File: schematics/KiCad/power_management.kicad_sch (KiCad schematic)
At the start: 33 parts, among them J3 USB_C, Q1 DMG6601LVT-7, Q2 DMG6601LVT-7, SW4 TL1105SF160R, U4 AP2112K-3.3, U5 MP2615AGQ-Z

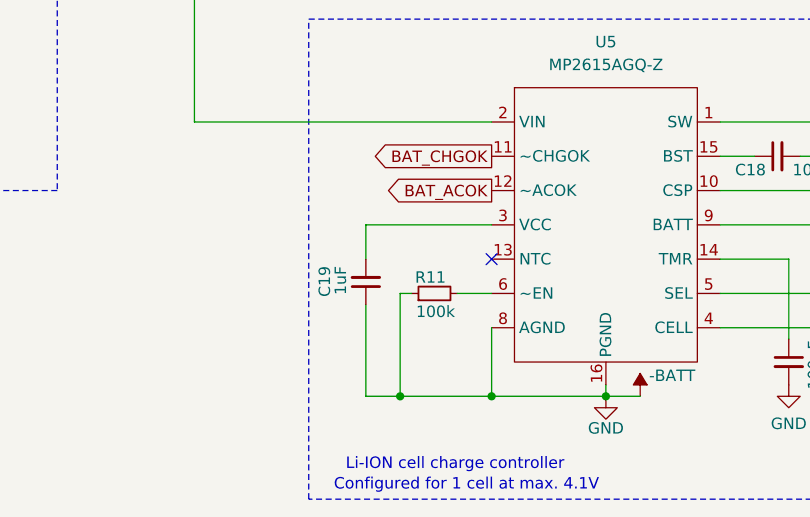
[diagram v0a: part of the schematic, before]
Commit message: wire up thermistor pin on charge controller
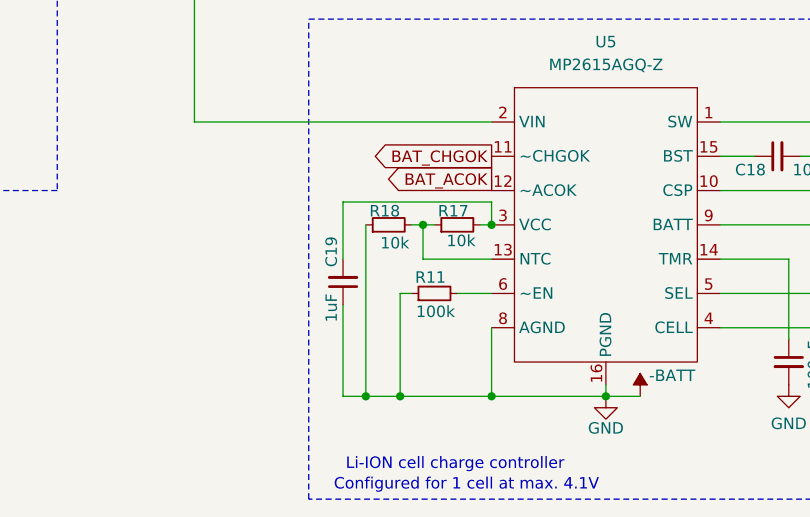
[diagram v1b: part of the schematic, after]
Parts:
- added R17, R18: 10k, Resistor_SMD:R_0603_1608Metric, symbol Device:R_Small
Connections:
- net -BATT: now also R18.1
- net at C19.2, U5.3 (VCC): now also R17.2
- net at U5.13 (NTC): now also R17.1, R18.2
- no-connect marks 1 -> 0
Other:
- moved on the sheet: C19

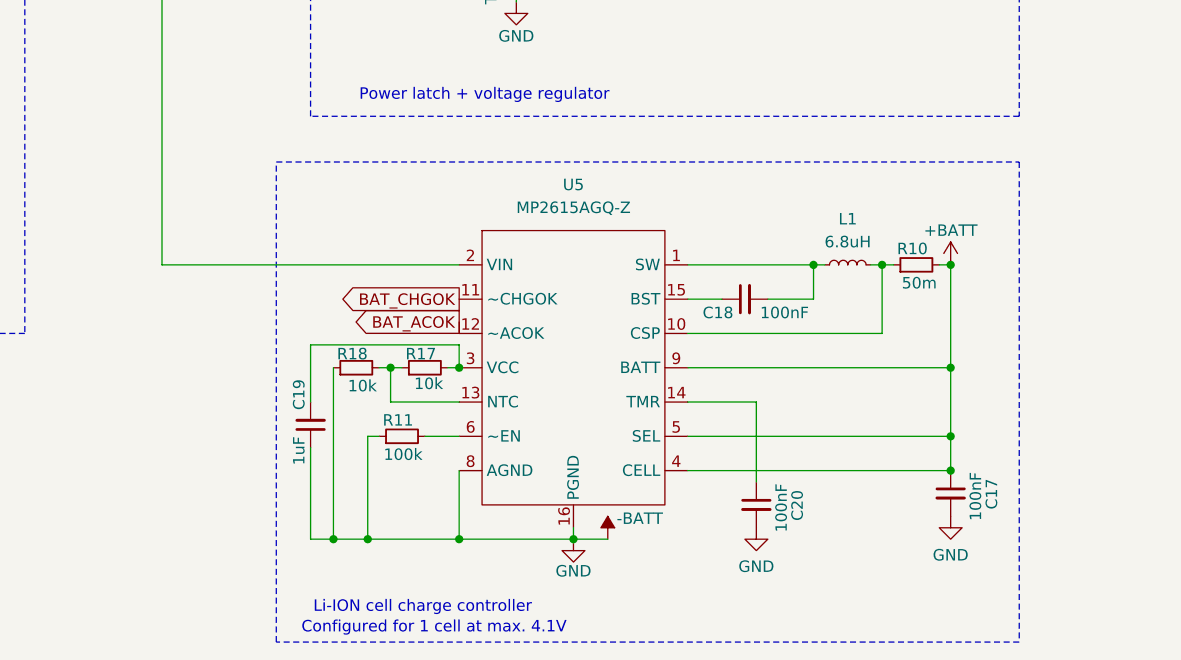
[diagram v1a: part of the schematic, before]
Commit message: set charge time according to datasheet
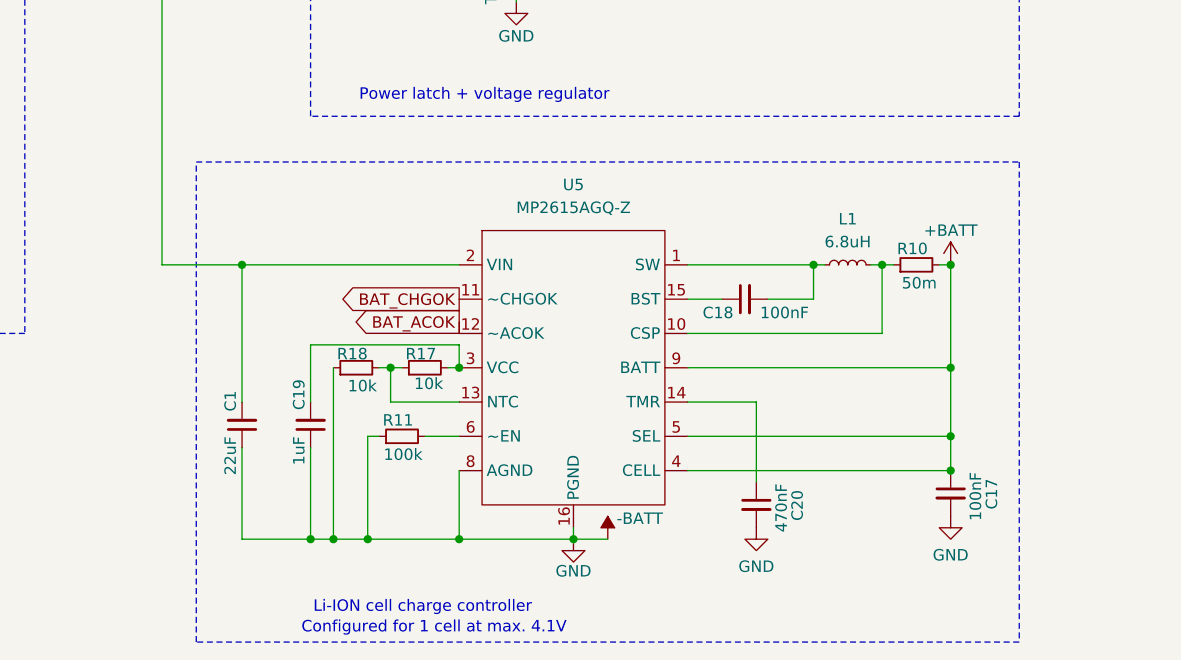
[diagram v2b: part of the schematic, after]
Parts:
- added C1: 22uF, Capacitor_SMD:C_0201_0603Metric, symbol Device:C_Small
- C20: value 100nF -> 470nF
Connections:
- net -BATT: now also C1.1
- net VBUS: now also C1.2
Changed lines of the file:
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@@
 	)
 	(junction
+		(at 100.33 115.57)
+		(diameter 0)
+		(color 0 0 0 0)
+	)
+	(junction
+		(at 107.95 146.05)
+		(diameter 0)
+		(color 0 0 0 0)
+	)
+	(junction
 		(at 91.44 74.93)
 		(diameter 0)
@@
 	(wire
 		(pts
-			(xy 91.44 115.57) (xy 124.46 115.57)
+			(xy 100.33 115.57) (xy 124.46 115.57)
+		)
+		(stroke
+			(width 0)
+			(type default)
+		)
+	)
+	(wire
+		(pts
+			(xy 91.44 115.57) (xy 100.33 115.57)
 		)
 		(stroke
@@
 	(wire
 		(pts
+			(xy 100.33 115.57) (xy 100.33 130.81)
+		)
+		(stroke
+			(width 0)
+			(type default)
+		)
+	)
+	(wire
+		(pts
 			(xy 55.88 90.17) (xy 57.15 90.17)
 		)
@@
 	(wire
 		(pts
+			(xy 100.33 135.89) (xy 100.33 146.05)
+		)
+		(stroke
+			(width 0)
+			(type default)
+		)
+	)
+	(wire
+		(pts
 			(xy 68.58 82.55) (xy 68.58 80.01)
 		)
@@
 	(wire
 		(pts
+			(xy 100.33 146.05) (xy 107.95 146.05)
+		)
+		(stroke
+			(width 0)
+			(type default)
+		)
+	)
+	(wire
+		(pts
 			(xy 140.97 85.09) (xy 140.97 83.82)
 		)
@@
 	)
 	(rectangle
-		(start 104.14 104.14)
+		(start 95.25 104.14)
 		(end 186.69 157.48)
 		(stroke
@@
 	)
 	(symbol
+		(lib_id "Device:C_Small")
+		(at 100.33 133.35 180)
+		(unit 1)
+		(exclude_from_sim no)
+		(in_bom yes)
+		(on_board yes)
+		(dnp no)
+		(property "Reference" "C1"
+			(at 99.06 129.54 90)
+			(effects
+				(font
+					(size 1.27 1.27)
+				)
+				(justify left)
+			)
+		)
+		(property "Value" "22uF"
+			(at 99.06 134.62 90)
+			(effects
+				(font
+					(size 1.27 1.27)
+				)
+				(justify left)
+			)
+		)
+		(property "Footprint" "Capacitor_SMD:C_0201_0603Metric"
+			(at 100.33 133.35 0)
+			(effects
+				(font
+					(size 1.27 1.27)
+				)
+				(hide yes)
+			)
+		)
+		(property "Datasheet" "~"
+			(at 100.33 133.35 0)
+			(effects
+				(font
+					(size 1.27 1.27)
+				)
+				(hide yes)
+			)
+		)
+		(property "Description" "Unpolarized capacitor, small symbol"
+			(at 100.33 133.35 0)
+			(effects
+				(font
+					(size 1.27 1.27)
+				)
+				(hide yes)
+			)
+		)
+		(pin "2"
+		)
+		(pin "1"
+		)
+		(instances
+			(project "leany"
+				(path "/e47b2519-93ca-4a48-9414-ecc253dd35f5/702fc064-eab2-4b82-8f62-a654ccd28f72"
+					(reference "C1")
+					(unit 1)
+				)
+			)
+		)
+	)
+	(symbol
 		(lib_id "Device:C_Polarized_Small")
 		(at 179.07 45.72 0)
@@
 			)
 		)
-		(property "Value" "100nF"
+		(property "Value" "470nF"
 			(at 160.274 145.288 90)
 			(effects

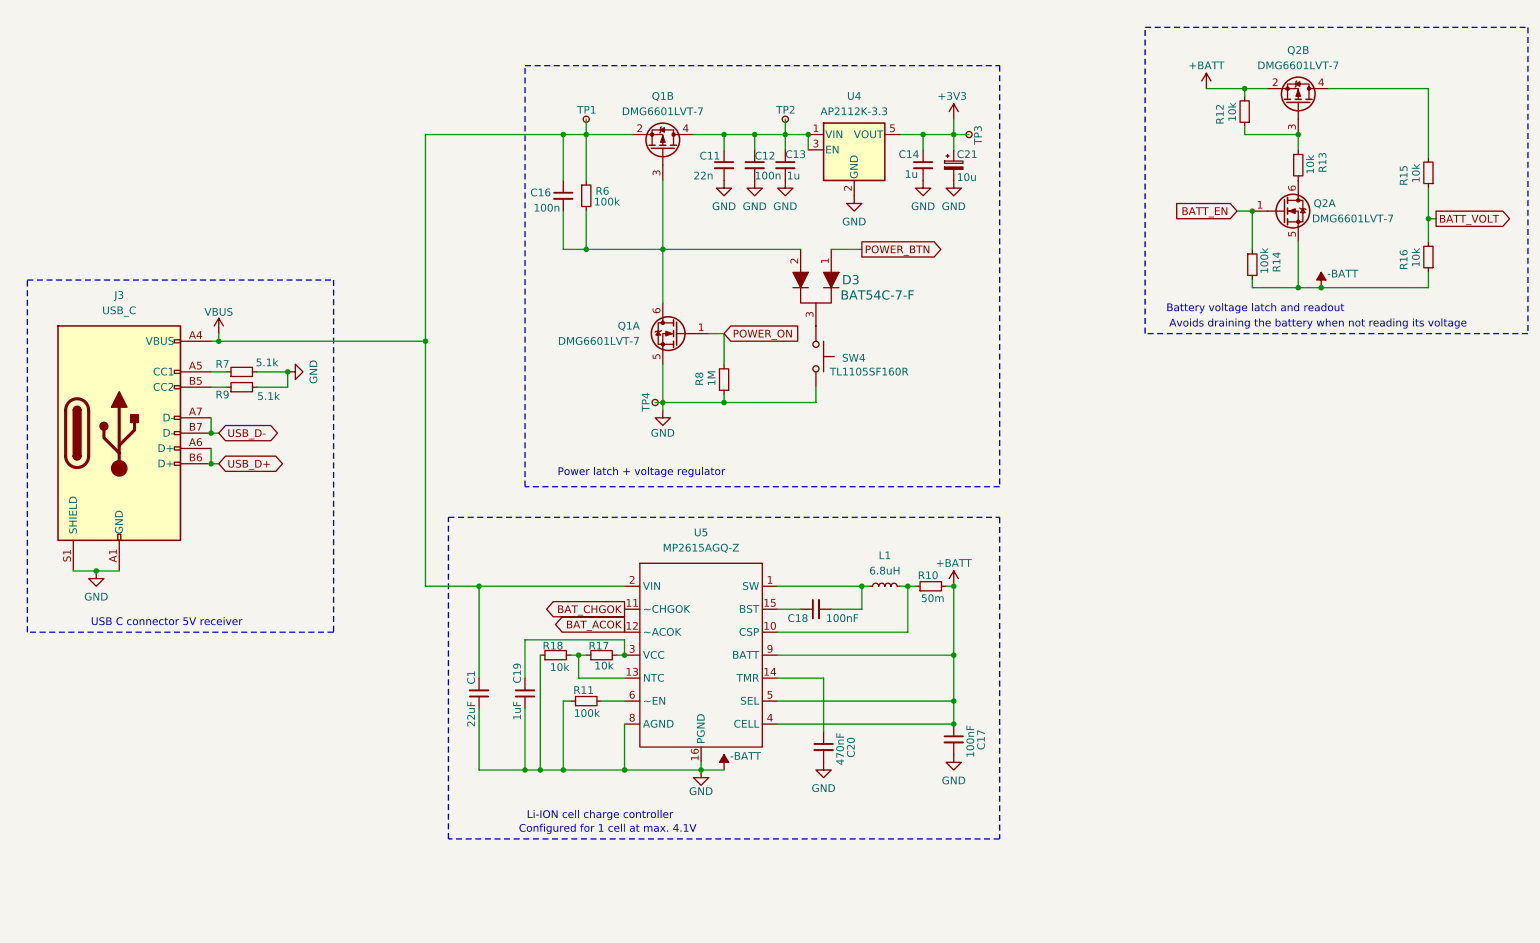
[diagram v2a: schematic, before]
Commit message: add decoupling and fix annotations
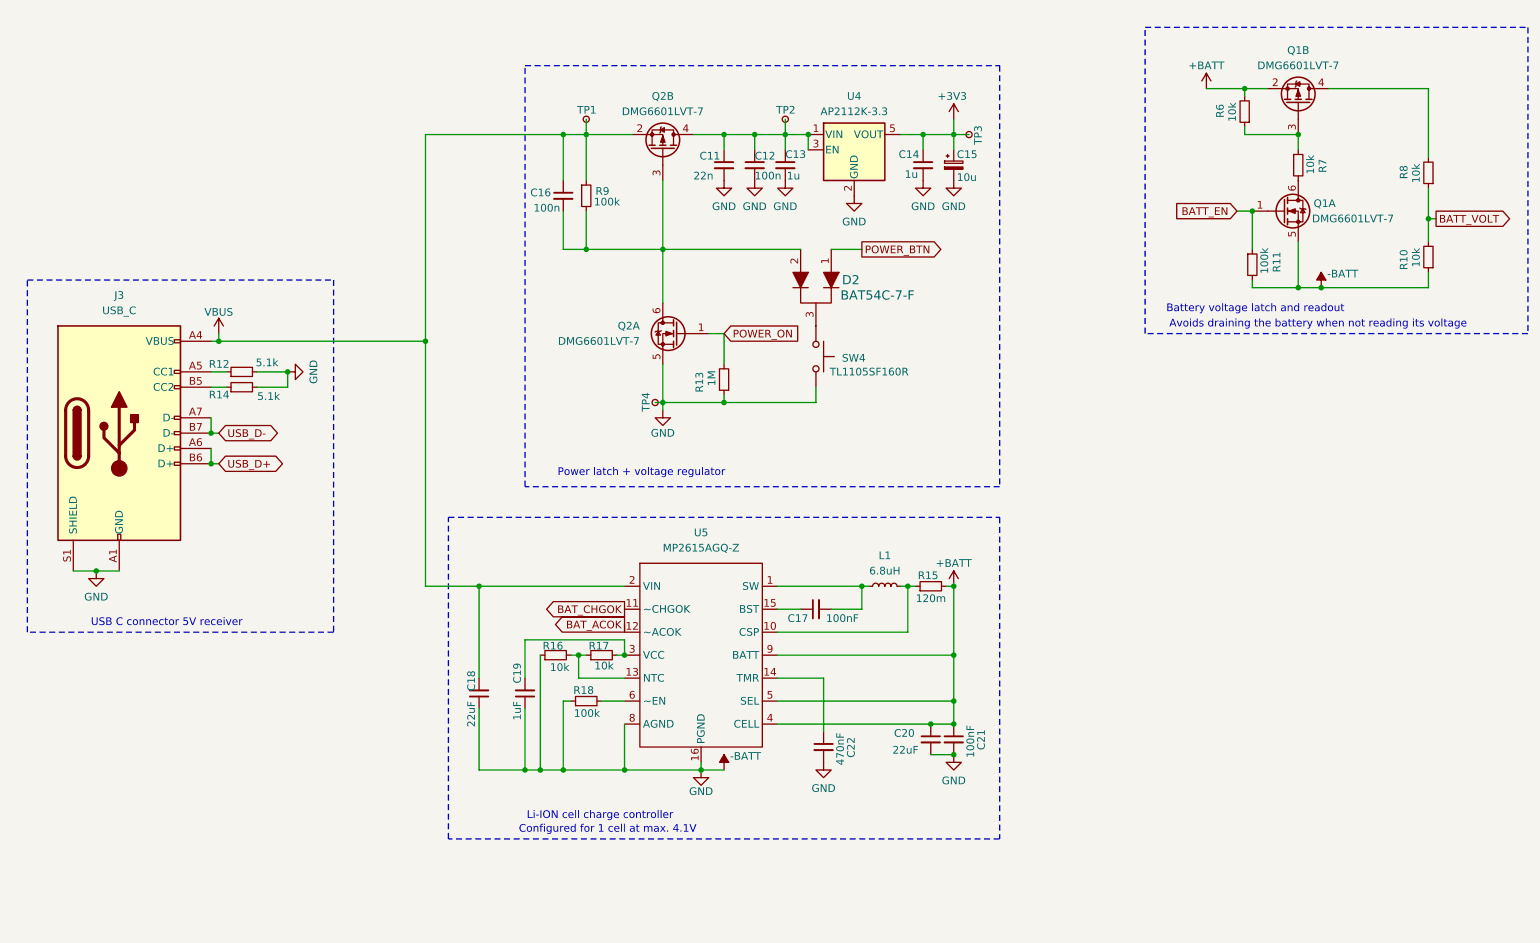
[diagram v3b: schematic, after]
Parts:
- added C20: 22uF, Capacitor_SMD:C_0201_0603Metric, symbol Device:C_Small
- R15: renamed from R10; value 50m -> 120m
- renumbered C21 to C15, C18 to C17, C1 to C18, C17 to C21, C20 to C22, D3 to D2, Q2 to Q1, Q1 to Q2, R16 to R10, R14 to R11, R7 to R12, R8 to R13, R9 to R14, R18 to R16, R11 to R18, R12 to R6, R13 to R7, R15 to R8, R6 to R9
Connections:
- net +BATT: now also C20.1
- net -BATT: now also C20.2

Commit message: add a test point at BATT+
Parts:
- added TP5: GND, TestPoint:TestPoint_Pad_1.0x1.0mm, symbol Connector:TestPoint_Small
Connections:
- net +BATT: now also TP5.1
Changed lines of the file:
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@@
+	(wire
+		(pts
+			(xy 179.07 115.57) (xy 181.61 115.57)
+		)
+		(stroke
+			(width 0)
+			(type default)
+		)
+	)
 	(wire
 		(pts
@@
 					(unit 1)
 				)
+			)
+		)
+	)
+	(symbol
+		(lib_id "Connector:TestPoint_Small")
+		(at 181.61 115.57 270)
+		(unit 1)
+		(exclude_from_sim no)
+		(in_bom yes)
+		(on_board yes)
+		(dnp no)
+		(property "Reference" "TP5"
+			(at 183.134 114.046 0)
+			(effects
+				(font
+					(size 1.27 1.27)
+				)
+				(justify left)
+			)
+		)
+		(property "Value" "GND"
+			(at 180.3401 116.84 0)
+			(effects
+				(font
+					(size 1.27 1.27)
+				)
+				(justify left)
+				(hide yes)
+			)
+		)
+		(property "Footprint" "TestPoint:TestPoint_Pad_1.0x1.0mm"
+			(at 181.61 120.65 0)
+			(effects
+				(font
+					(size 1.27 1.27)
+				)
+				(hide yes)
+			)
+		)
+		(property "Datasheet" "~"
+			(at 181.61 120.65 0)
+			(effects
+				(font
+					(size 1.27 1.27)
+				)
+				(hide yes)
+			)
+		)
+		(property "Description" "test point"
+			(at 181.61 115.57 0)
+			(effects
+				(font
+					(size 1.27 1.27)
+				)
+				(hide yes)
+			)
+		)
+		(pin "1"
+		)
+		(instances
+			(project "leany"
+				(path "/e47b2519-93ca-4a48-9414-ecc253dd35f5/702fc064-eab2-4b82-8f62-a654ccd28f72"
+					(reference "TP5")
+					(unit 1)
+				)

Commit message: add a test point at battery voltage ADC input
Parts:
- added TP6: GND, TestPoint:TestPoint_Pad_1.0x1.0mm, symbol Connector:TestPoint_Small
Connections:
- net BATT_VOLT: now also TP6.1
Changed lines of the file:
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@@
 	)
 	(junction
+		(at 257.81 57.15)
+		(diameter 0)
+		(color 0 0 0 0)
+	)
+	(junction
 		(at 154.94 40.64)
 		(diameter 0)
@@
 	(wire
 		(pts
+			(xy 257.81 57.15) (xy 260.35 57.15)
+		)
+		(stroke
+			(width 0)
+			(type default)
+		)
+	)
+	(wire
+		(pts
 			(xy 100.33 115.57) (xy 100.33 130.81)
 		)
@@
 	(wire
 		(pts
-			(xy 257.81 54.61) (xy 257.81 58.42)
+			(xy 257.81 54.61) (xy 257.81 57.15)
 		)
 		(stroke
@@
 	(wire
 		(pts
+			(xy 257.81 57.15) (xy 257.81 58.42)
+		)
+		(stroke
+			(width 0)
+			(type default)
+		)
+	)
+	(wire
+		(pts
 			(xy 55.88 90.17) (xy 55.88 87.63)
 		)
@@
 					(unit 1)
 				)
+			)
+		)
+	)
+	(symbol
+		(lib_id "Connector:TestPoint_Small")
+		(at 260.35 57.15 270)
+		(unit 1)
+		(exclude_from_sim no)
+		(in_bom yes)
+		(on_board yes)
+		(dnp no)
+		(property "Reference" "TP6"
+			(at 261.112 57.404 90)
+			(effects
+				(font
+					(size 1.27 1.27)
+				)
+				(justify left)
+			)
+		)
+		(property "Value" "GND"
+			(at 259.0801 58.42 0)
+			(effects
+				(font
+					(size 1.27 1.27)
+				)
+				(justify left)
+				(hide yes)
+			)
+		)
+		(property "Footprint" "TestPoint:TestPoint_Pad_1.0x1.0mm"
+			(at 260.35 62.23 0)
+			(effects
+				(font
+					(size 1.27 1.27)
+				)
+				(hide yes)
+			)
+		)
+		(property "Datasheet" "~"
+			(at 260.35 62.23 0)
+			(effects
+				(font
+					(size 1.27 1.27)
+				)
+				(hide yes)
+			)
+		)
+		(property "Description" "test point"
+			(at 260.35 57.15 0)
+			(effects
+				(font
+					(size 1.27 1.27)
+				)
+				(hide yes)
+			)
+		)
+		(pin "1"
+		)
+		(instances
+			(project "leany"
+				(path "/e47b2519-93ca-4a48-9414-ecc253dd35f5/702fc064-eab2-4b82-8f62-a654ccd28f72"
+					(reference "TP6")
+					(unit 1)
+				)
